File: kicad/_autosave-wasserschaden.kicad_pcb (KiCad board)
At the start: 2 copper layers, 50.8 x 50.2 mm, 13 parts, among them J1 valve out, J2 12V in, U1 stepdown, U2 WeMos_mini

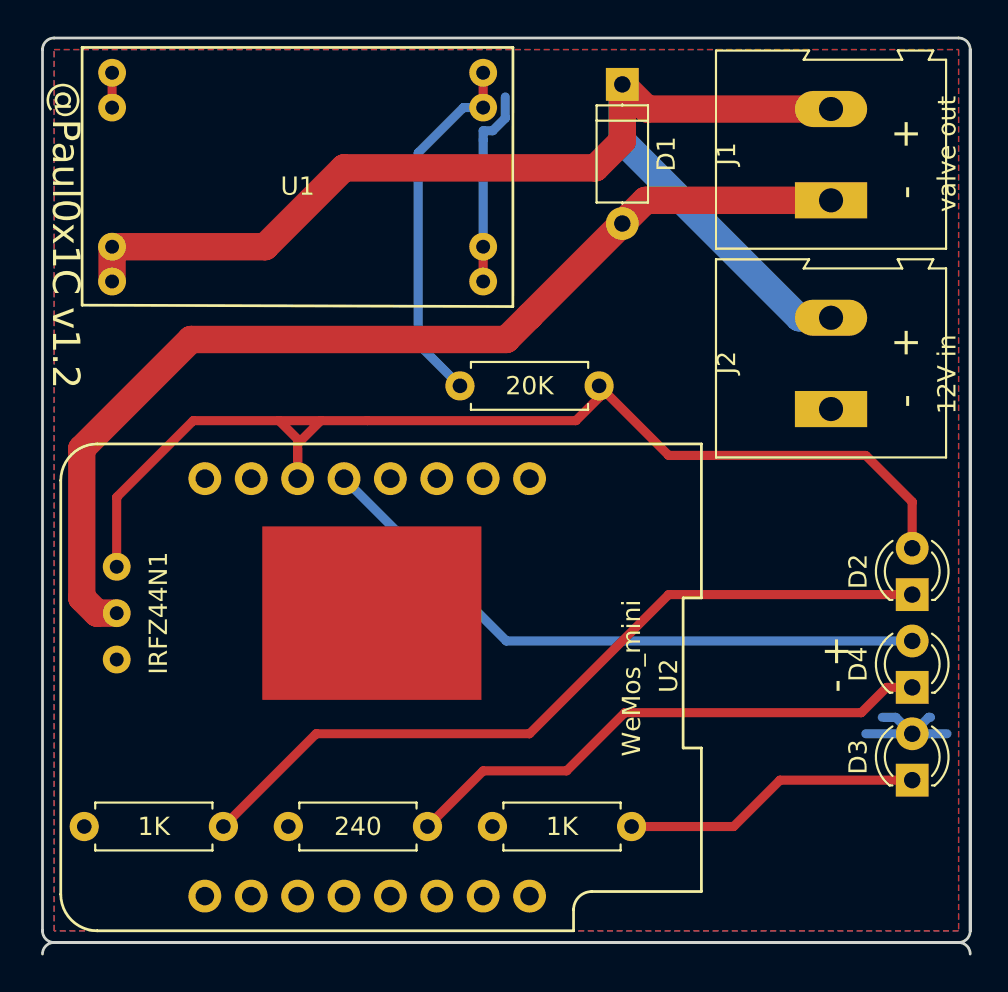
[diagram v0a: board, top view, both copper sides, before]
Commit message: added deepsleep jumper to schematic &cleanup
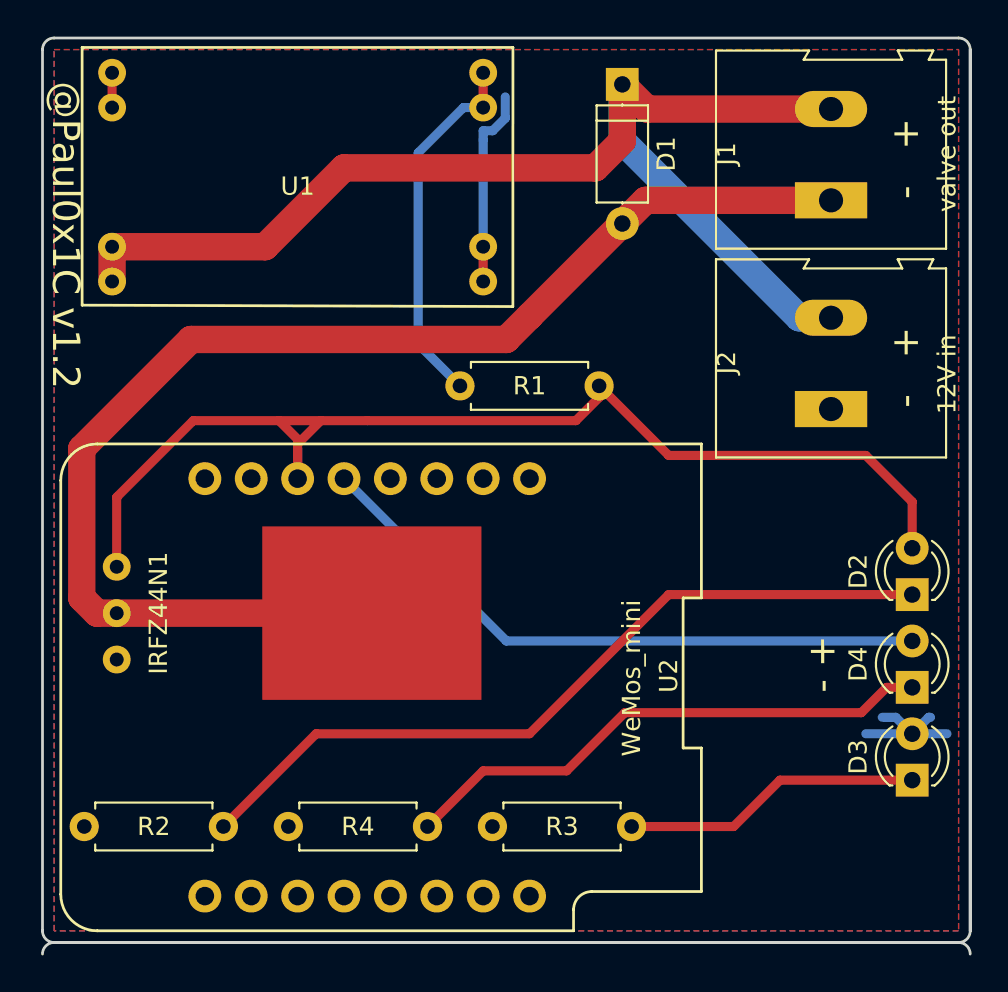
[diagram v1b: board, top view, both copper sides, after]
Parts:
- renumbered 20K to R1, 1K to R2, 1K to R3, 240 to R4
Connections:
- D3 pad 2: +3V3 -> Net-(D3-Pad2)
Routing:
- net Net-(D1-Pad2): track 57.1 -> 71.1 mm
- net Net-(D3-Pad2): track 0.00 -> 7.84 mm
- net +3V3: track 18.8 -> 10.9 mm
